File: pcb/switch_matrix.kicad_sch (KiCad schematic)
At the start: 21 parts, among them U1 SN74LVC1G139, U2 TLP161J, U3 TLP161J, U4 TLP161J, U5 TLP161J, U6 TLP161J, U7 TLP161J

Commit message: WiP level control
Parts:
- R3, R4, R5, R6, R7, R8: value 170 -> 180
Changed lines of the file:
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@@
       (effects (font (size 1.27 1.27)))
     )
-    (property "Value" "170" (at 168.91 59.69 90)
+    (property "Value" "180" (at 168.91 59.69 90)
       (effects (font (size 1.27 1.27)))
     )
@@
       (effects (font (size 1.27 1.27)))
     )
-    (property "Value" "170" (at 168.91 123.19 90)
+    (property "Value" "180" (at 168.91 123.19 90)
       (effects (font (size 1.27 1.27)))
     )
@@
       (effects (font (size 1.27 1.27)))
     )
-    (property "Value" "170" (at 168.91 106.68 90)
+    (property "Value" "180" (at 168.91 106.68 90)
       (effects (font (size 1.27 1.27)))
     )
@@
       (effects (font (size 1.27 1.27)))
     )
-    (property "Value" "170" (at 168.91 143.51 90)
+    (property "Value" "180" (at 168.91 143.51 90)
       (effects (font (size 1.27 1.27)))
     )
@@
       (effects (font (size 1.27 1.27)))
     )
-    (property "Value" "170" (at 168.91 74.93 90)
+    (property "Value" "180" (at 168.91 74.93 90)
       (effects (font (size 1.27 1.27)))
     )
@@
       (effects (font (size 1.27 1.27)))
     )
-    (property "Value" "170" (at 168.91 90.17 90)
-      (effects (font (size 1.27 1.27)))
-    )
+    (property "Value" "180" (at 168.91 90.17 90)
+      (effects (font (size 1.27 1.27)))
+    )

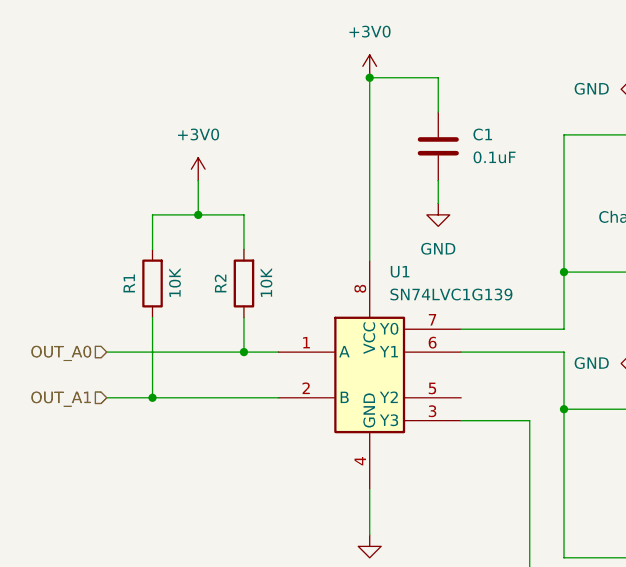
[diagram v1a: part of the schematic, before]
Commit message: Added pulse control harmonized resistor values
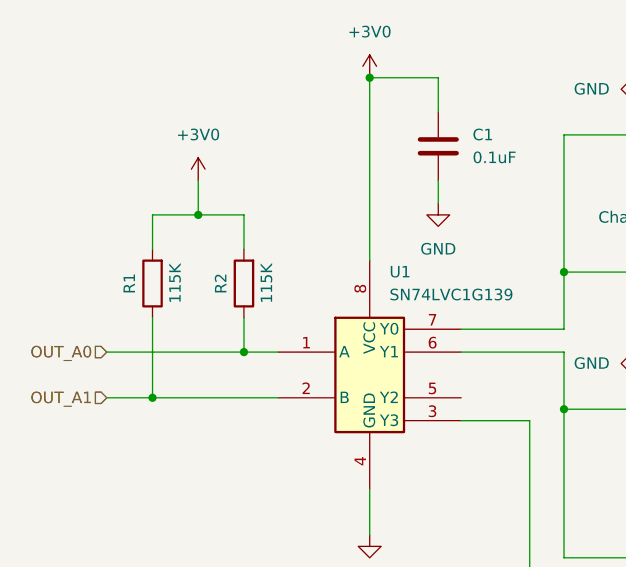
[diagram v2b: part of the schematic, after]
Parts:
- R1, R2: value 10K -> 115K
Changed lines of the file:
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@@
       (effects (font (size 1.27 1.27)))
     )
-    (property "Value" "10K" (at 105.41 78.74 90)
+    (property "Value" "115K" (at 105.41 78.74 90)
       (effects (font (size 1.27 1.27)))
     )
@@
       (effects (font (size 1.27 1.27)) hide)
     )
-    (property "Datasheet" "" (at 116.84 88.9 0)
+    (property "Datasheet" "http://www.ti.com/lit/sg/scyt129e/scyt129e.pdf" (at 116.84 88.9 0)
       (effects (font (size 1.27 1.27)) hide)
     )
@@
       (effects (font (size 1.27 1.27)))
     )
-    (property "Value" "10K" (at 95.25 78.74 90)
-      (effects (font (size 1.27 1.27)))
-    )
+    (property "Value" "115K" (at 95.25 78.74 90)
+      (effects (font (size 1.27 1.27)))
+    )
